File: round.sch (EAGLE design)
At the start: 8 parts, among them IC1 MC9S08GT8A-48, U1 USD-SOCKETNEW, U2 MCP73831, U3 ADXL345, U5 RFM69CW

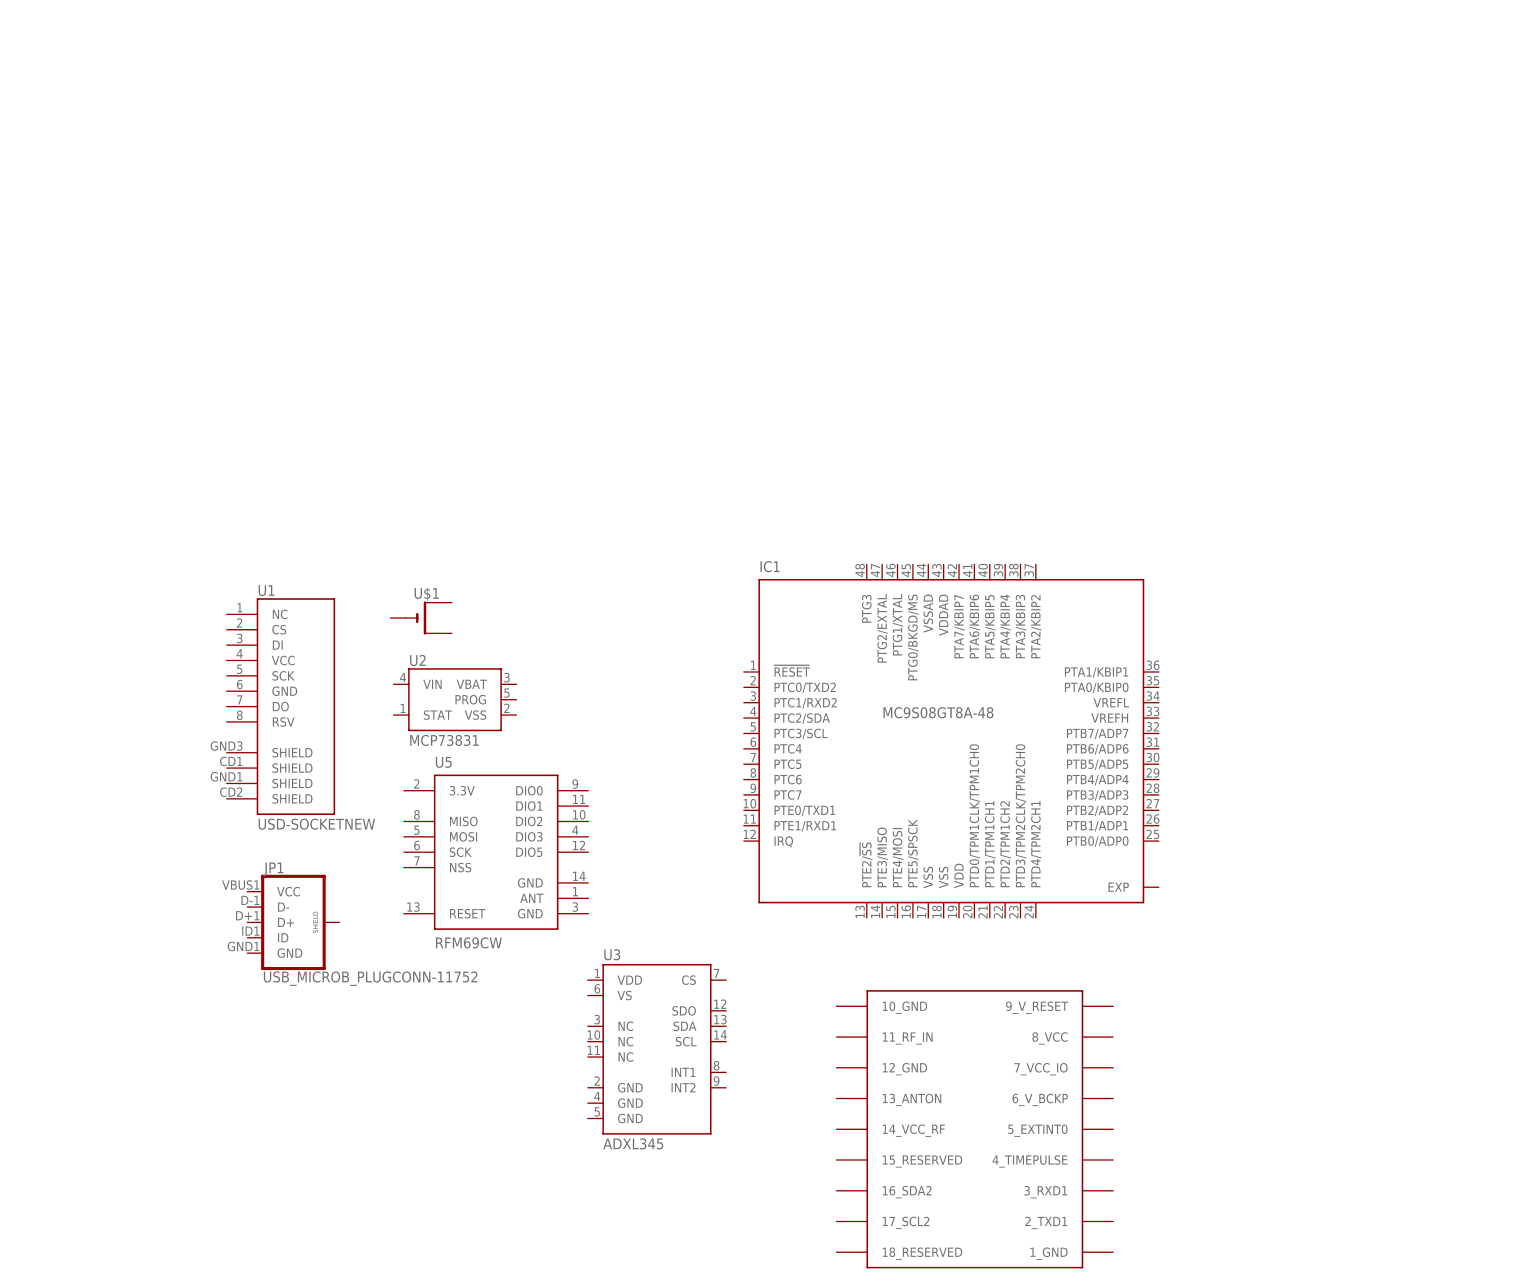
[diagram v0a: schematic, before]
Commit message: Added power supply to round boards.
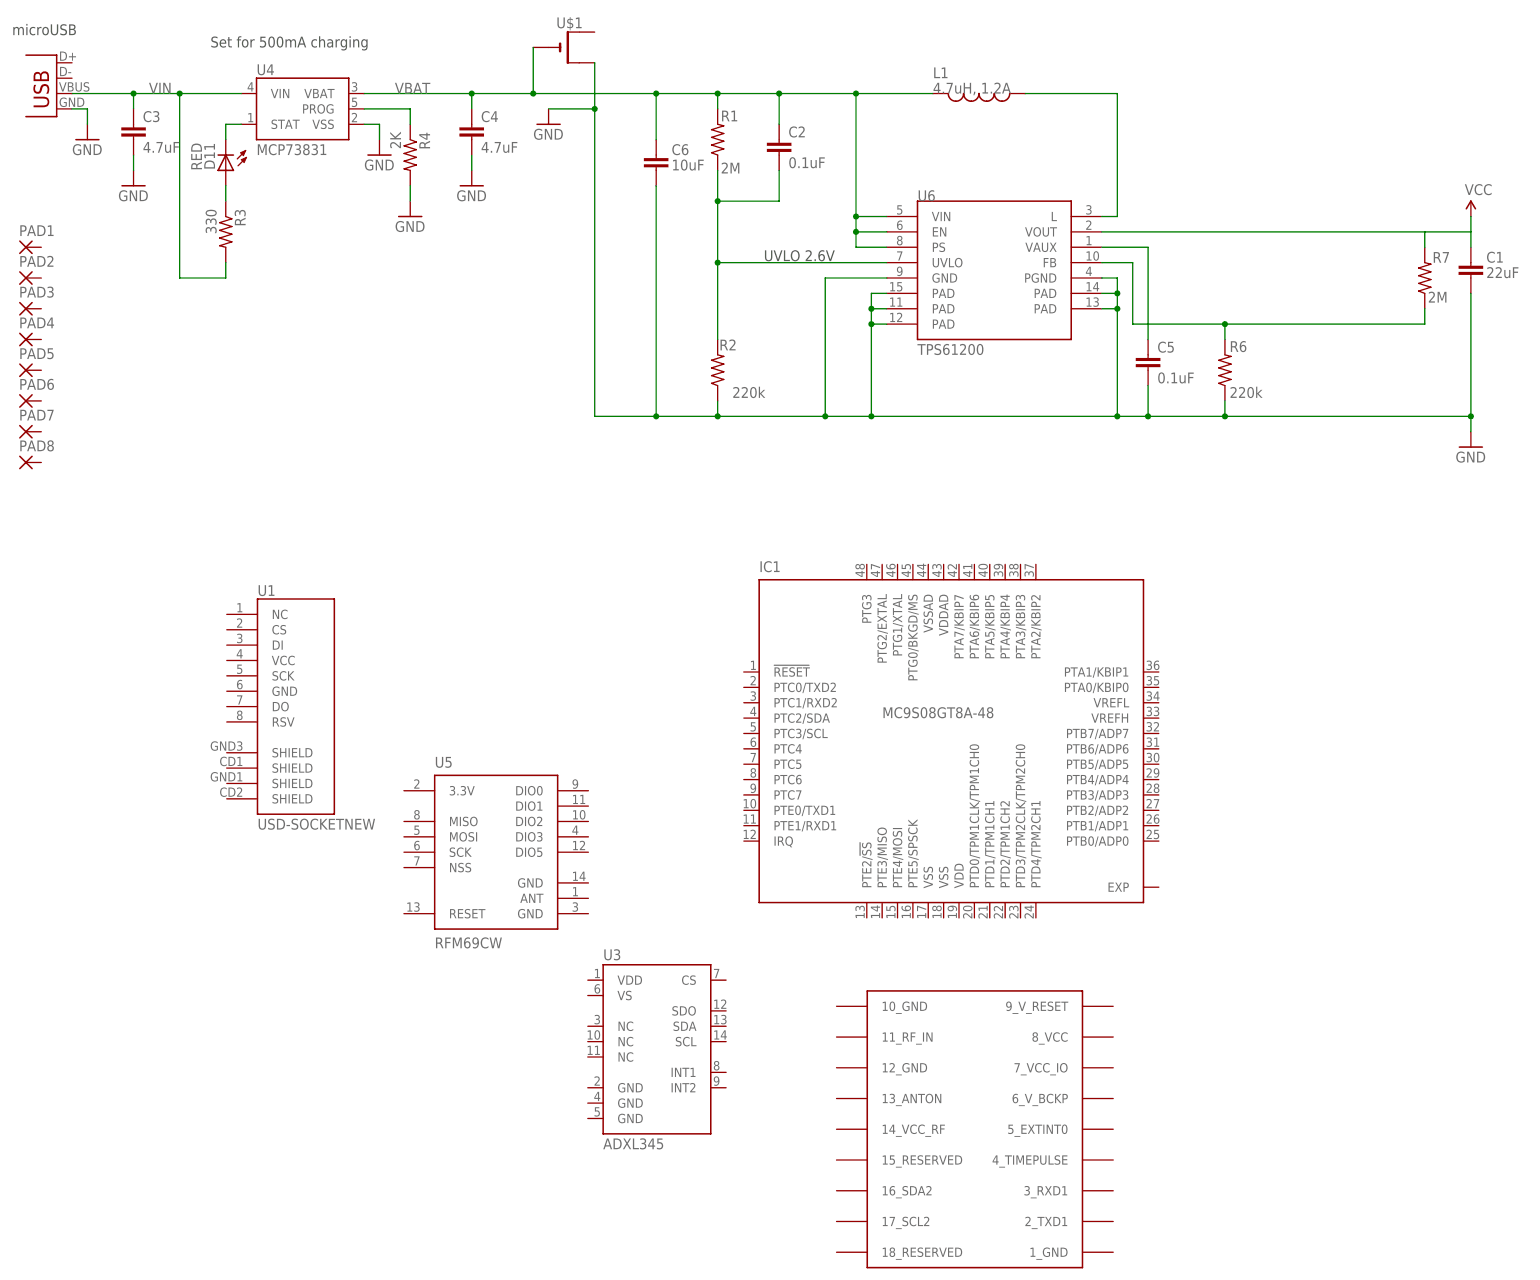
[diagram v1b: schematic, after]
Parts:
- removed JP1: USB_MICROB_PLUGCONN-11752, SparkFun-Connectors:USB_MICROB_PLUGCONN-11752
- removed U2: MCP73831, SparkFun-PowerIC:MCP73831
- added C1: 22uF, CH_passive:CAP0805
- added C2, C5: 0.1uF, SparkFun:CAP0603-CAP
- added C3, C4: 4.7uF, SparkFun:CAP0402-CAP
- added C6: 10uF, CH_passive:CAP1206
- added D11: RED, SparkFun:LED0603
- added L1: 4.7uH, 1.2A, SparkFun:INDUCTOR.
- added PAD1, PAD2, PAD3, PAD4, PAD5, PAD6, PAD7, PAD8: (no value), wirepad:2,15/1,0
- added R1, R7: 2M, SparkFun:RESISTOR0603-RES
- added R2, R6: 220k, SparkFun:RESISTOR0603-RES
- added R3: 330, SparkFun:RESISTOR0402-RES
- added R4: 2K, SparkFun:RESISTOR0402-RES
- added U4: MCP73831, SparkFun:MCP73831
- added U6: TPS61200, SparkFun:TPS61200
- added X1: Micro USB, SparkFun:USB-MICROB
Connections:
- new net FB: R6.2, R7.1, U6.FB
- new net GND: C1.2, C3.2, C4.2, C5.2, C6.2, R2.1, R4.2, R6.1, U$1.+1, U4.VSS, U6.GND, U6.PAD@1, U6.PAD@2, U6.PAD@3, U6.PAD@4, U6.PAD@5, U6.PGND, X1.GND
- new net N$1: C5.1, U6.VAUX
- new net N$2: L1.1, U6.L
- new net N$3: D11.A, R3.1
- new net PROG: R4.1, U4.PROG
- new net STAT: D11.C, U4.STAT
- new net UVLO: C2.2, R1.1, R2.2, U6.UVLO
- new net VBAT: C2.1, C4.1, C6.1, L1.2, R1.2, U$1.-, U4.VBAT, U6.EN, U6.PS, U6.VIN
- new net VCC: C1.1, R7.2, U6.VOUT
- new net VIN: C3.1, R3.2, U4.VIN, X1.VBUS
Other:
- note added: "Set for 500mA charging"
- note added: "UVLO 2.6V"
- note added: "microUSB"
- moved on the sheet: U$1
